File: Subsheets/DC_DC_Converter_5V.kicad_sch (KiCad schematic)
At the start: 30 parts

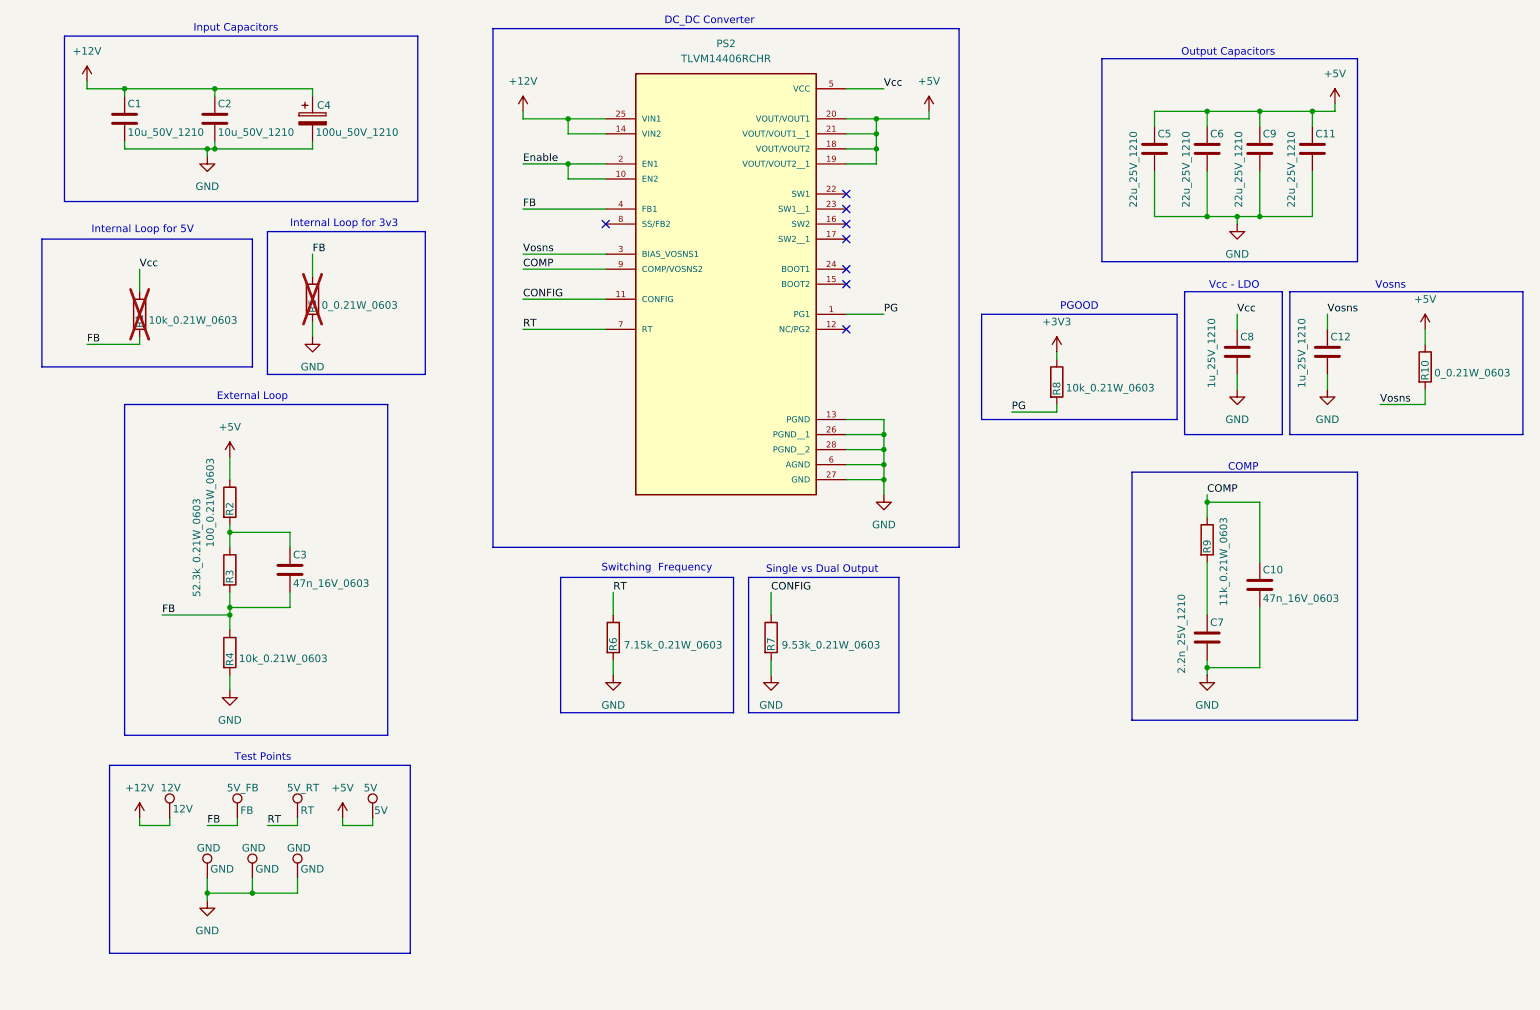
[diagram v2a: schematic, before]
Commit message: Layout  closed, some DRC  conflicts remain.
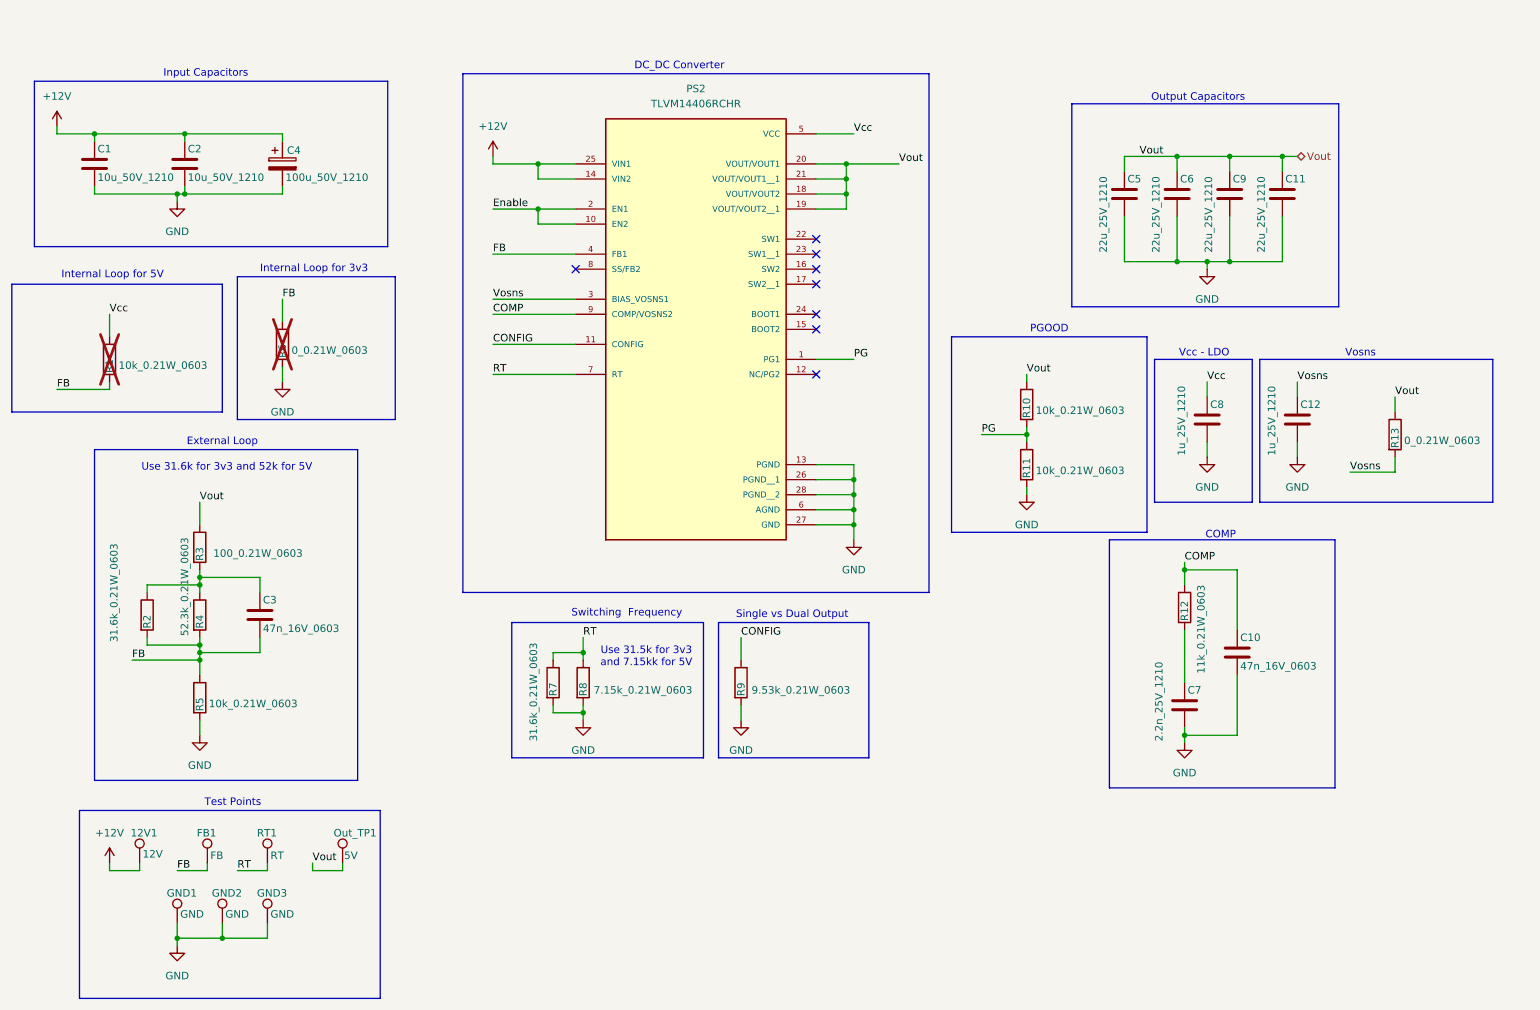
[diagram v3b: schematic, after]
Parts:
- removed 12V: 12V, TestPoint:TestPoint_Pad_2.0x2.0mm, symbol Connector:TestPoint
- removed 5V: 5V, TestPoint:TestPoint_Pad_2.0x2.0mm, symbol Connector:TestPoint
- removed 5V_FB: FB, TestPoint:TestPoint_Pad_2.0x2.0mm, symbol Connector:TestPoint
- removed 5V_RT: RT, TestPoint:TestPoint_Pad_2.0x2.0mm, symbol Connector:TestPoint
- removed GND (x3): GND, TestPoint:TestPoint_Pad_2.0x2.0mm, symbol Connector:TestPoint
- added 12V1: 12V, TestPoint:TestPoint_Pad_2.0x2.0mm, symbol Connector:TestPoint
- added FB1: FB, TestPoint:TestPoint_Pad_2.0x2.0mm, symbol Connector:TestPoint
- added GND1, GND2, GND3: GND, TestPoint:TestPoint_Pad_2.0x2.0mm, symbol Connector:TestPoint
- added Out_TP1: 5V, TestPoint:TestPoint_Pad_2.0x2.0mm, symbol Connector:TestPoint
- added R11: 10k_0.21W_0603, Resistor_SMD:R_0603_1608Metric_Pad0.98x0.95mm_HandSolder, symbol Device:R
- added R12: 11k_0.21W_0603, Resistor_SMD:R_0603_1608Metric_Pad0.98x0.95mm_HandSolder, symbol Device:R
- added R13: 0_0.21W_0603, Resistor_SMD:R_0603_1608Metric_Pad0.98x0.95mm_HandSolder, symbol Device:R
- added RT1: RT, TestPoint:TestPoint_Pad_2.0x2.0mm, symbol Connector:TestPoint
- R10: value 0_0.21W_0603 -> 10k_0.21W_0603; Manufacturer Part Number CRCW06030000Z0EAHP -> CRCW060310K0FKEAHP; Price 4.86 -> 6.01; Vendor Link https://www.digikey.in/en/products/detail/vishay-dale/CRCW06030000Z0EAHP/2222231https://www.digikey.in/en/products/detail/vishay-dale/CRCW06030000Z0EAHP/2222231 -> https://www.digikey.in/en/products/detail/vishay-dale/CRCW060310K0FKEAHP/2222263; Vendor Part Number 541-0.0SBCT-ND -> 541-10.0KSCT-ND
- R2: value 100_0.21W_0603 -> 31.6k_0.21W_0603; Manufacturer Part Number CRCW0603100RFKEAHP -> CRCW060331K6FKEAC; Price 6.01 -> 2.56; Vendor Link https://www.digikey.in/en/products/detail/vishay-dale/CRCW0603100RFKEAHP/2222245 -> https://www.digikey.in/en/products/detail/vishay-dale/CRCW060331K6FKEAC/7924046; Vendor Part Number 541-100SCT-ND -> 541-5351-1-ND
- R3: value 52.3k_0.21W_0603 -> 100_0.21W_0603; Manufacturer Part Number CRCW060352K3FKEAC -> CRCW0603100RFKEAHP; Price 2.56 -> 6.01; Vendor Link https://www.digikey.in/en/products/detail/vishay-dale/CRCW060352K3FKEAC/7924235 -> https://www.digikey.in/en/products/detail/vishay-dale/CRCW0603100RFKEAHP/2222245; Vendor Part Number 541-5470-1-ND -> 541-100SCT-ND
- R4: value 10k_0.21W_0603 -> 52.3k_0.21W_0603; Manufacturer Part Number CRCW060310K0FKEAHP -> CRCW060352K3FKEAC; Price 6.01 -> 2.56; Vendor Link https://www.digikey.in/en/products/detail/vishay-dale/CRCW060310K0FKEAHP/2222263 -> https://www.digikey.in/en/products/detail/vishay-dale/CRCW060352K3FKEAC/7924235; Vendor Part Number 541-10.0KSCT-ND -> 541-5470-1-ND
- R5: value 0_0.21W_0603 -> 10k_0.21W_0603; Manufacturer Part Number CRCW06030000Z0EAHP -> CRCW060310K0FKEAHP; Price 4.86 -> 6.01; Vendor Link https://www.digikey.in/en/products/detail/vishay-dale/CRCW06030000Z0EAHP/2222231 -> https://www.digikey.in/en/products/detail/vishay-dale/CRCW060310K0FKEAHP/2222263; Vendor Part Number 541-0.0SBCT-ND -> 541-10.0KSCT-ND; now fitted
- R6: value 7.15k_0.21W_0603 -> 0_0.21W_0603; Manufacturer Part Number CRCW06037K15FKEAHP -> CRCW06030000Z0EAHP; Price 6.9 -> 4.86; Vendor Link https://www.digikey.in/en/products/detail/vishay-dale/CRCW06037K15FKEAHP/2226271 -> https://www.digikey.in/en/products/detail/vishay-dale/CRCW06030000Z0EAHP/2222231; Vendor Part Number 541-CRCW06037K15FKEAHPCT-ND -> 541-0.0SBCT-ND; now not fitted
- R7: value 9.53k_0.21W_0603 -> 31.6k_0.21W_0603; Manufacturer Part Number CRCW06039K53FKEAC -> CRCW060331K6FKEAC; Vendor Link https://www.digikey.in/en/products/detail/vishay-dale/CRCW06039K53FKEAC/7924391 -> https://www.digikey.in/en/products/detail/vishay-dale/CRCW060331K6FKEAC/7924046; Vendor Part Number 541-5606-1-ND -> 541-5351-1-ND
- R8: value 10k_0.21W_0603 -> 7.15k_0.21W_0603; Manufacturer Part Number CRCW060310K0FKEAHP -> CRCW06037K15FKEAHP; Price 6.01 -> 6.9; Vendor Link https://www.digikey.in/en/products/detail/vishay-dale/CRCW060310K0FKEAHP/2222263 -> https://www.digikey.in/en/products/detail/vishay-dale/CRCW06037K15FKEAHP/2226271; Vendor Part Number 541-10.0KSCT-ND -> 541-CRCW06037K15FKEAHPCT-ND
- R9: value 11k_0.21W_0603 -> 9.53k_0.21W_0603; Manufacturer Part Number CRCW060311K0FKEAC -> CRCW06039K53FKEAC; Vendor Link https://www.digikey.in/en/products/detail/vishay-dale/CRCW060311K0FKEAC/7924120 -> https://www.digikey.in/en/products/detail/vishay-dale/CRCW06039K53FKEAC/7924391; Vendor Part Number 541-5146-1-ND -> 541-5606-1-ND
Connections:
- net +3V3 is gone; now on net RT: R8.1
- net +12V: now also 12V1.1
- net COMP: now also R12.1; no longer R9.1
- net CONFIG: now also R9.1; no longer R7.1
- net FB: now also R2.2, R4.2, R6.1, FB1.1; no longer R3.2, R4.1
- net GND: now also R8.2, R9.2, GND1.1, GND2.1, GND3.1, R11.2; no longer R4.2
- net PG: now also R10.2, R11.1; no longer R8.2
- net RT: now also R7.1, RT1.1; no longer R6.1
- net Vosns: now also R13.2; no longer R10.2
- net at C7.1: now also R12.2; no longer R9.2
- net +5V renamed Vout
- net Vout: now also R3.1, Out_TP1.1, R13.1; no longer R2.1
- new net: C3.1, R2.1, R3.2, R4.1
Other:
- note added: "Use 31.5k for 3v3 and 7.15kk for 5V"
- note added: "Use 31.6k for 3v3 and 52k for 5V"
